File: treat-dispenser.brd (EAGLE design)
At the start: 88.9 x 44.5 mm, 32 parts, among them U1 MCP73831, U2 TPS6103x, Y1 16MHz

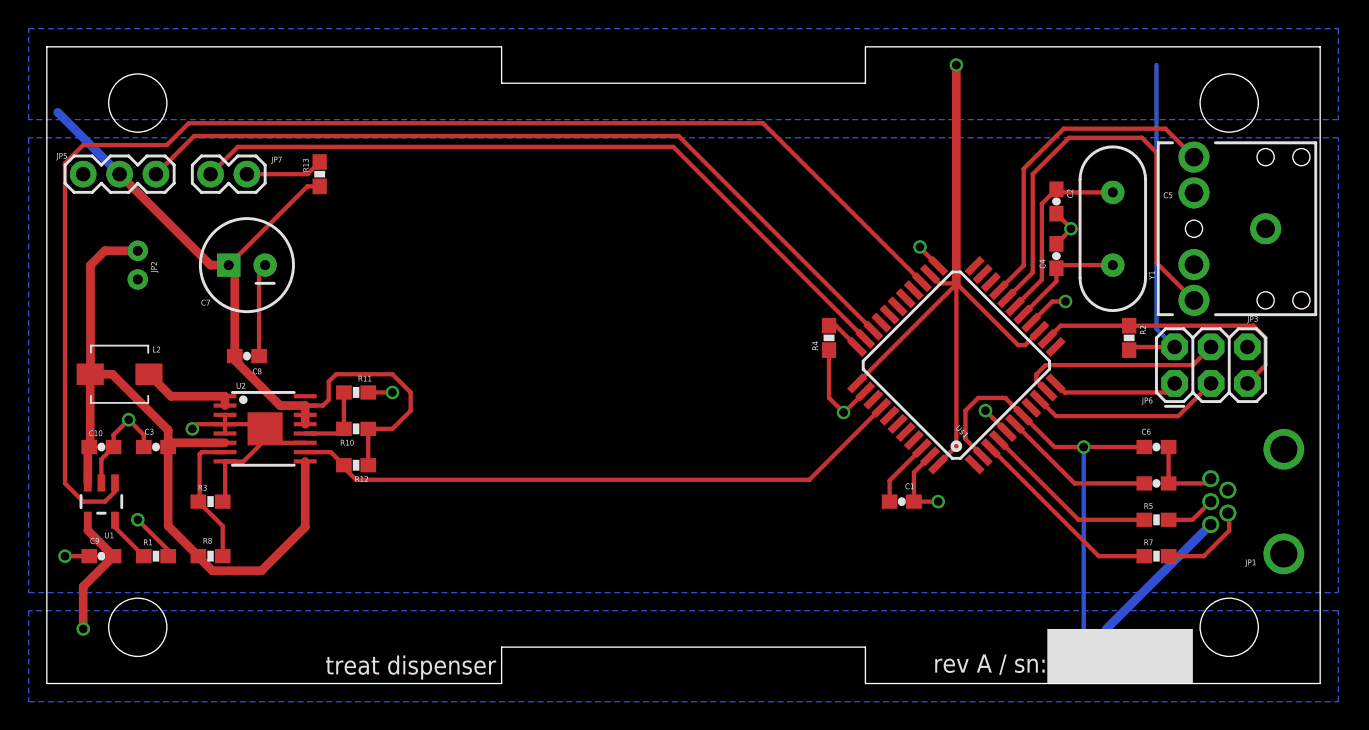
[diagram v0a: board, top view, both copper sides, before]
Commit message: moved servo to clear path for battery connector
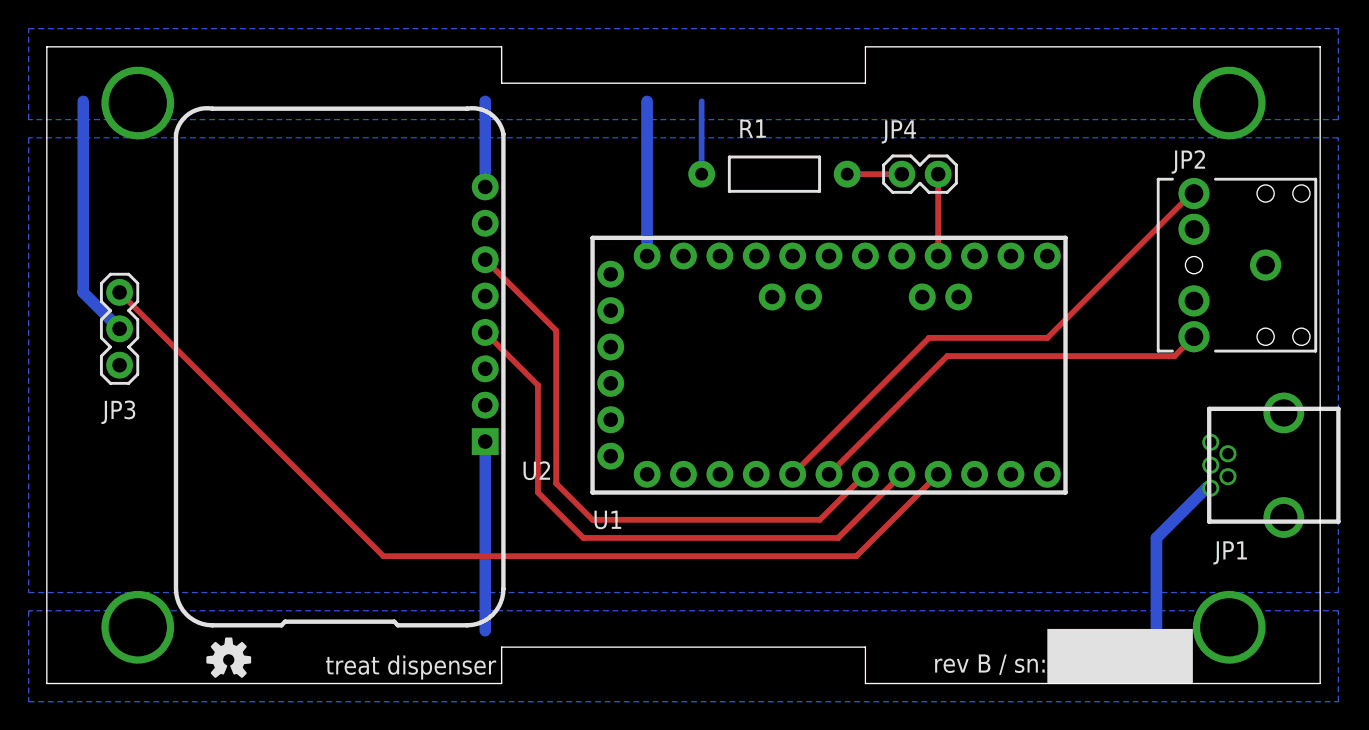
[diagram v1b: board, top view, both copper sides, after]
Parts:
- removed C1: 0.1uF, SparkFun:0603-CAP
- removed C10, C9: 4.7uF, SparkFun:0603-CAP
- removed C2, C4: 22pF, SparkFun:0603-CAP
- removed C3, C8: 10uF, SparkFun:0603-CAP
- removed C5, C6: 1uF, SparkFun:0603-CAP
- removed C7: 220uF, SparkFun-Capacitors:CPOL-RADIAL-100UF-25V
- removed JP5: (no value), SparkFun-Connectors:1X03
- removed JP6: (no value), SparkFun-Connectors:2X3
- removed JP7: (no value), SparkFun-Connectors:1X02
- removed L2: (no value), SparkFun-Passives:INDUCTOR-SRP4020
- removed R10, R12, R8: 1M, SparkFun:0603-RES
- removed R11: 110K, SparkFun:0603-RES
- removed R13: 470, SparkFun:0603-RES
- removed R2, R4: 10K, SparkFun:0603-RES
- removed R3: 182K, SparkFun:0603-RES
- removed R5, R7: 22, SparkFun:0603-RES
- removed U$1: ATMEGA32U4TQFP-44, SparkFun-DigitalIC:TQFP44
- removed Y1: 16MHz, SparkFun:HC49US
- added JP4: (no value), SparkFun-Connectors:1X02
- added LOGO1: OSHW-LOGOS, SparkFun-Aesthetics:OSHW-LOGO-S
- JP2: device SparkFun-Connectors:JST-2-PTH-KIT -> SparkFun-Connectors:AUDIO-JACK
- JP3: device SparkFun-Connectors:AUDIO-JACK -> SparkFun-Connectors:1X03
- R1: value 10K -> 470; device SparkFun:0603-RES -> SparkFun:AXIAL-0.4
- U1: value MCP73831 -> ARDUINO_PRO_MINI; device SparkFun:SOT23-5 -> SparkFun-Boards:ARDUINO_PRO_MINI
- U2: value TPS6103x -> PB1000; device tps6103x:TSSOP-16 -> powerboost:PB1000
- moved JP3 80.6 mm to (5.08, 22.2), turned to 90 degrees
- moved JP2 78.7 mm to (85.1, 29.2), turned to 180 degrees
- moved U1 51.7 mm to (54.6, 22.2), turned to 90 degrees
- moved R1 50.8 mm to (50.8, 35.6)
- moved U2 21.6 mm to (31.9, 4.06), turned to 90 degrees
- moved JP1 2.54 mm to (86.4, 15.2)
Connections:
- removed net A0: U$1.36
- removed net A1: R12.2, U$1.37, U2.10
- removed net A2: U$1.38
- removed net A3: U$1.39
- removed net A4: U$1.40
- removed net A5: U$1.41
- removed net AREF: C1.2, U$1.42
- removed net D+: JP1.D+, R5.2
- removed net D-: JP1.D-, R7.2
- removed net D10: U$1.30
- removed net D11: U$1.12
- removed net D12: U$1.26
- removed net D13: JP7.1, U$1.32
- removed net D14: U$1.8
- removed net D2: JP3.TIP, U$1.19
- removed net D3: JP3.RING, U$1.18
- removed net D4: U$1.25, U1.1
- removed net D5: JP5.3, U$1.31
- removed net D6: U$1.27
- removed net D7: U$1.1
- removed net D8: U$1.28
- removed net D9: U$1.29
- removed net FB: R10.2, R11.1, U2.12
- removed net LBI: R3.1, R8.1, U2.7
- removed net MISO: JP6.1, U$1.11
- removed net MOSI: JP6.4, U$1.10
- removed net N$1: C4.1, U$1.16, Y1.1
- removed net N$2: C2.1, U$1.17, Y1.2
- removed net N$3: U$1.22
- removed net N$4: C5.2, U$1.6
- removed net N$5: R4.2, U$1.33
- removed net PROG: R1.1, U1.5
- removed net RD+: R5.1, U$1.4
- removed net RD-: R7.1, U$1.3
- removed net RESET: JP6.5, R2.1, U$1.13
- removed net RXI: U$1.20
- removed net SCK: JP6.3, U$1.9
- removed net SW: L2.P$2, U2.1, U2.2
- removed net TXO: U$1.21
- removed net UVCC: C6.2, C9.1, JP1.VBUS, U$1.2, U$1.7, U1.4
- removed net VCC: C7.1, C8.1, JP5.2, JP6.2, R10.1, R12.1, R13.1, R2.2, U$1.14, U$1.24, U$1.34, U$1.44, U2.13, U2.14, U2.15
- removed net V_BATT: C10.1, C3.1, JP2.2, L2.P$1, R8.2, U1.3, U2.6, U2.9
- new net 5V: JP3.2, R1.P$1, U1.24, U2.P8
- new net B1: JP2.TIP, U1.5
- new net B2: JP2.RING, U1.6
- new net EN: U1.8, U2.P4
- new net LBO: U1.7, U2.P6
- new net LED: JP4.1, U1.16
- new net SERVO: JP3.3, U1.9
- new net VBUS: JP1.VBUS, U2.P1
- net GND: now also JP2.SLEEVE, JP3.1, U1.23, U1.4, U2.P5, U2.P7; no longer C1.1, C10.2, C2.2, C3.2, C4.2, C5.1, C6.1, C7.2, C8.2, C9.2, JP2.1, JP3.SLEEVE, JP5.1, JP6.6, R1.2, R11.2, R3.2, R4.1, U$1.15, U$1.23, U$1.35, U$1.43, U$1.5, U1.2, U2.11, U2.3, U2.4, U2.5, U2.8, U2.PAD
- net N$8: now also JP4.2, R1.P$2; no longer JP7.2, R13.2
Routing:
- net VCC: track 128.0 -> 0.00 mm, vias 1 -> 0
- net D4: track 93.2 -> 0.00 mm
- net SERVO: track 0.00 -> 67.1 mm
- net GND: track 65.3 -> 0.00 mm, vias 11 -> 0
- net D5: track 56.8 -> 0.00 mm
- net V_BATT: track 53.7 -> 0.00 mm
- net D13: track 52.0 -> 0.00 mm
- net UVCC: track 50.2 -> 0.00 mm, vias 2 -> 0
- net A1: track 43.2 -> 0.00 mm
- net LBO: track 0.00 -> 41.6 mm
- net EN: track 0.00 -> 41.3 mm
- net 5V: track 0.00 -> 38.8 mm
- net B1: track 0.00 -> 36.1 mm
- net D3: track 30.9 -> 0.00 mm
- net B2: track 0.00 -> 29.5 mm
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- added copper zone on layer 16, net 5V
- added copper zone on layer 16, net VBUS
- removed copper zone on layer 16, net UVCC
- removed copper zone on layer 16, net VCC
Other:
- outline, holes or cut-outs redrawn
- board text added: "rev B / sn:"
- board text removed: "rev A / sn:"

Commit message: rev C update: - added dedicated battery connector - reversed led polarity - added enable switch - removed en connection to arduino - added status led and lbo to arduino code
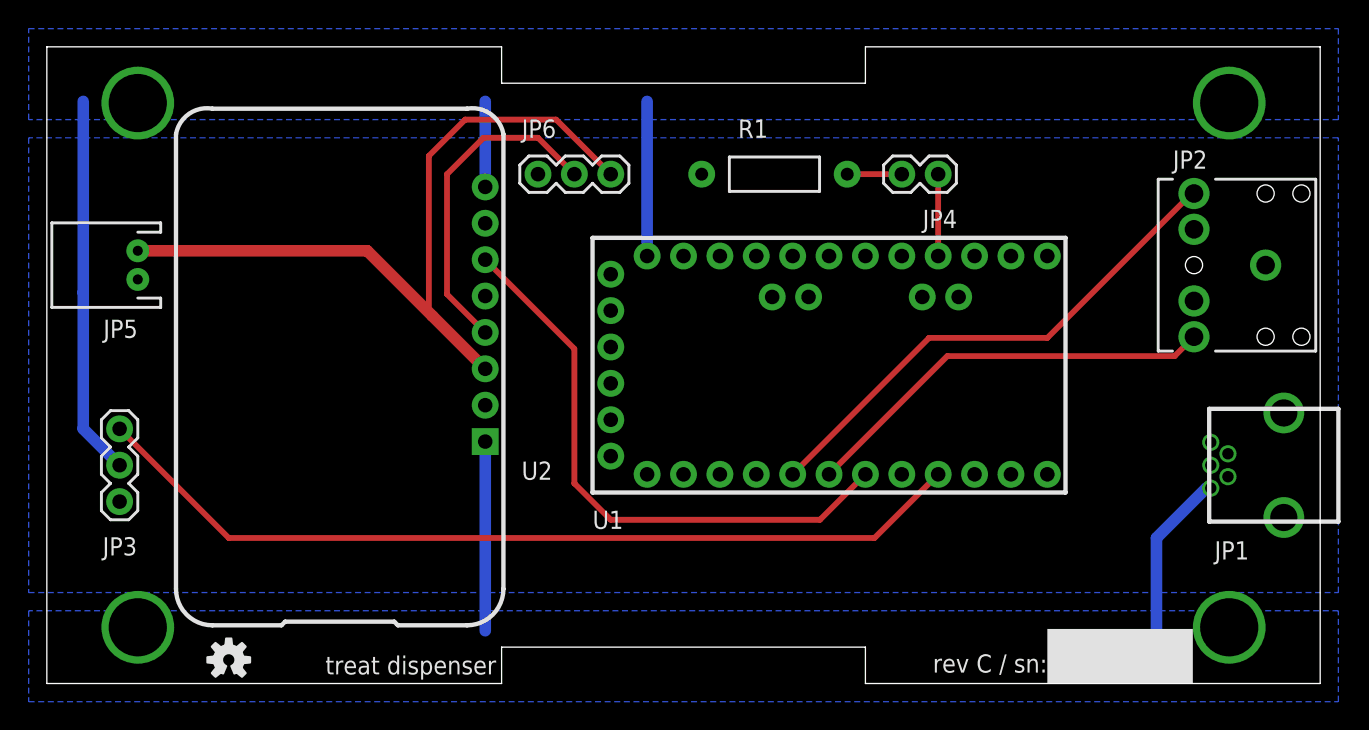
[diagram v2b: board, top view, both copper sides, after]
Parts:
- added JP5: (no value), SparkFun-Connectors:JST-2-PTH
- added JP6: (no value), SparkFun-Connectors:1X03
- moved JP3 9.53 mm to (5.08, 12.7)
- moved JP4 2.54 mm to (59.7, 35.6), turned to 0 degrees
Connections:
- removed net N$8: JP4.2, R1.P$2
- new net N$5: JP4.1, R1.P$2
- new net VBAT: JP5.2, JP6.3, U2.P3
- net 5V: no longer R1.P$1
- net EN: now also JP6.2; no longer U1.8
- net GND: now also JP5.1, JP6.1, R1.P$1
- net LED: now also JP4.2; no longer JP4.1
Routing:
- net VBAT: track 0.00 -> 54.3 mm
- net EN: track 41.3 -> 23.1 mm
- net SERVO: track 67.1 -> 62.1 mm
- net 5V: track 38.8 -> 43.2 mm
- net N$8: track 3.81 -> 0.00 mm
- net N$5: track 0.00 -> 3.81 mm
- net LBO: track 41.6 -> 40.9 mm
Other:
- board text added: "rev C / sn:"
- board text removed: "rev B / sn:"
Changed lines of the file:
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@@
 <board>
 <plain>
-<text x="69.85" y="2.032" size="1.27" layer="21" font="vector" rot="R180">rev B / sn:</text>
+<text x="69.85" y="2.032" size="1.27" layer="21" font="vector" rot="R180">rev C / sn:</text>
 <text x="31.369" y="1.905" size="1.27" layer="21" font="vector" rot="R180">treat dispenser</text>
 <rectangle x1="69.85" y1="0" x2="80.01" y2="3.81" layer="21" rot="R180"/>
@@
 <attribute name="VALUE" x="86.36" y="27.94" size="0.4064" layer="27" rot="R180"/>
 </element>
-<element name="JP3" library="SparkFun-Connectors" package="1X03" value="" x="5.08" y="22.225" smashed="yes" rot="R90">
-<attribute name="PN" value="952-1312-ND" x="5.08" y="22.225" size="1.778" layer="27" rot="R90" display="off"/>
-<attribute name="NAME" x="6.2992" y="18.4658" size="1.27" layer="25" font="vector" align="bottom-right"/>
-<attribute name="VALUE" x="8.255" y="20.955" size="1.27" layer="27" rot="R90"/>
-</element>
-<element name="JP4" library="SparkFun-Connectors" package="1X02" value="" x="62.23" y="35.56" smashed="yes" rot="R180">
-<attribute name="PN" value="952-1311-ND" x="62.23" y="35.56" size="1.778" layer="27" rot="R180" display="off"/>
-<attribute name="NAME" x="58.3692" y="38.0492" size="1.27" layer="25" font="vector"/>
-<attribute name="VALUE" x="63.5" y="38.735" size="1.27" layer="27" rot="R180"/>
+<element name="JP3" library="SparkFun-Connectors" package="1X03" value="" x="5.08" y="12.7" smashed="yes" rot="R90">
+<attribute name="PN" value="952-1312-ND" x="5.08" y="12.7" size="1.778" layer="27" rot="R90" display="off"/>
+<attribute name="NAME" x="6.2992" y="8.9408" size="1.27" layer="25" font="vector" align="bottom-right"/>
+<attribute name="VALUE" x="8.255" y="11.43" size="1.27" layer="27" rot="R90"/>
+</element>
+<element name="JP4" library="SparkFun-Connectors" package="1X02" value="" x="59.69" y="35.56" smashed="yes">
+<attribute name="PN" value="952-1311-ND" x="59.69" y="35.56" size="1.778" layer="27" display="off"/>
+<attribute name="NAME" x="63.5508" y="33.0708" size="1.27" layer="25" font="vector" rot="R180"/>
+<attribute name="VALUE" x="58.42" y="32.385" size="1.27" layer="27"/>
 </element>
 <element name="R1" library="SparkFun" package="AXIAL-0.4" value="470" x="50.8" y="35.56" smashed="yes">
@@
 </element>
 <element name="LOGO1" library="SparkFun-Aesthetics" package="OSHW-LOGO-S" value="OSHW-LOGOS" x="12.7" y="1.651"/>
+<element name="JP5" library="SparkFun-Connectors" package="JST-2-PTH" value="" x="6.35" y="29.21" smashed="yes" rot="R90">
+<attribute name="SKU" value="PRT-09914" x="6.35" y="29.21" size="1.778" layer="27" rot="R90" display="off"/>
+<attribute name="PROD_ID" value="CONN-09863" x="6.35" y="29.21" size="1.778" layer="27" rot="R90" display="off"/>
+<attribute name="NAME" x="6.35" y="25.4" size="1.27" layer="25" font="vector" rot="R180"/>
+<attribute name="VALUE" x="2.35" y="27.94" size="0.4064" layer="27" rot="R90"/>
+<attribute name="PN" value="455-1719-ND" x="6.35" y="29.21" size="1.778" layer="27" rot="R90" display="off"/>
+</element>
+<element name="JP6" library="SparkFun-Connectors" package="1X03" value="" x="34.29" y="35.56" smashed="yes">
+<attribute name="PN" value="EG1903-ND" x="34.29" y="35.56" size="1.778" layer="27" display="off"/>
+<attribute name="NAME" x="35.56" y="39.37" size="1.27" layer="25" font="vector" rot="R180"/>
+<attribute name="VALUE" x="33.02" y="32.385" size="1.27" layer="27"/>
+</element>
 </elements>
 <signals>
@@
 <contactref element="U2" pad="P7"/>
 <contactref element="JP1" pad="GND"/>
+<contactref element="R1" pad="P$1"/>
+<contactref element="JP5" pad="1"/>
+<contactref element="JP6" pad="1"/>
 </signal>
 <signal name="SERVO">
 <contactref element="JP3" pad="3"/>
 <contactref element="U1" pad="9"/>
-<wire x1="62.23" y1="14.605" x2="56.515" y2="8.89" width="0.4064" layer="1"/>
-<wire x1="5.08" y1="27.305" x2="23.495" y2="8.89" width="0.4064" layer="1"/>
-<wire x1="23.495" y1="8.89" x2="56.515" y2="8.89" width="0.4064" layer="1"/>
+<wire x1="62.23" y1="14.605" x2="57.785" y2="10.16" width="0.4064" layer="1"/>
+<wire x1="57.785" y1="10.16" x2="12.7" y2="10.16" width="0.4064" layer="1"/>
+<wire x1="5.08" y1="17.78" x2="12.7" y2="10.16" width="0.4064" layer="1"/>
 </signal>
 <signal name="N$9">
 </signal>
 <signal name="N$10">
-</signal>
-<signal name="N$8">
-<contactref element="R1" pad="P$2"/>
-<contactref element="JP4" pad="2"/>
-<wire x1="59.69" y1="35.56" x2="55.88" y2="35.56" width="0.4064" layer="1"/>
 </signal>
 <signal name="5V">
 <contactref element="JP3" pad="2"/>
 <contactref element="U2" pad="P8"/>
-<contactref element="R1" pad="P$1"/>
 <contactref element="U1" pad="24"/>
 <polygon width="0.3556" layer="16">
@@
 </polygon>
 <wire x1="41.91" y1="29.845" x2="41.91" y2="40.64" width="0.8128" layer="16"/>
-<wire x1="45.72" y1="35.56" x2="45.72" y2="40.64" width="0.4064" layer="16"/>
 <wire x1="30.607" y1="34.671" x2="30.607" y2="40.64" width="0.8128" layer="16"/>
-<wire x1="5.08" y1="24.765" x2="2.54" y2="27.305" width="0.8128" layer="16"/>
 <wire x1="2.54" y1="27.305" x2="2.54" y2="40.64" width="0.8128" layer="16"/>
+<wire x1="2.54" y1="27.305" x2="2.54" y2="17.78" width="0.8128" layer="16"/>
+<wire x1="2.54" y1="17.78" x2="5.08" y2="15.24" width="0.8128" layer="16"/>
 </signal>
 <signal name="B2">
@@
 </signal>
 <signal name="LED">
-<contactref element="JP4" pad="1"/>
 <contactref element="U1" pad="16"/>
+<contactref element="JP4" pad="2"/>
 <wire x1="62.23" y1="35.56" x2="62.23" y2="29.845" width="0.4064" layer="1"/>
 </signal>
@@
 <contactref element="U1" pad="7"/>
 <wire x1="57.15" y1="14.605" x2="53.975" y2="11.43" width="0.4064" layer="1"/>
-<wire x1="30.607" y1="29.591" x2="35.56" y2="24.638" width="0.4064" layer="1"/>
-<wire x1="35.56" y1="24.638" x2="35.56" y2="13.97" width="0.4064" layer="1"/>
-<wire x1="53.975" y1="11.43" x2="38.1" y2="11.43" width="0.4064" layer="1"/>
-<wire x1="38.1" y1="11.43" x2="35.56" y2="13.97" width="0.4064" layer="1"/>
-</signal>
-<signal name="EN">
-<contactref element="U2" pad="P4"/>
-<contactref element="U1" pad="8"/>
-<wire x1="59.69" y1="14.605" x2="55.245" y2="10.16" width="0.4064" layer="1"/>
-<wire x1="30.607" y1="24.511" x2="34.29" y2="20.828" width="0.4064" layer="1"/>
-<wire x1="55.245" y1="10.16" x2="37.465" y2="10.16" width="0.4064" layer="1"/>
-<wire x1="37.465" y1="10.16" x2="34.29" y2="13.335" width="0.4064" layer="1"/>
-<wire x1="34.29" y1="13.335" x2="34.29" y2="20.828" width="0.4064" layer="1"/>
+<wire x1="53.975" y1="11.43" x2="39.37" y2="11.43" width="0.4064" layer="1"/>
+<wire x1="39.37" y1="11.43" x2="36.83" y2="13.97" width="0.4064" layer="1"/>
+<wire x1="36.83" y1="13.97" x2="36.83" y2="23.368" width="0.4064" layer="1"/>
+<wire x1="36.83" y1="23.368" x2="30.607" y2="29.591" width="0.4064" layer="1"/>
+</signal>
+<signal name="VBAT">
+<contactref element="U2" pad="P3"/>
+<contactref element="JP5" pad="2"/>
+<contactref element="JP6" pad="3"/>
+<wire x1="6.35" y1="30.21" x2="22.368" y2="30.21" width="0.8128" layer="1"/>
+<wire x1="22.368" y1="30.21" x2="26.924" y2="25.654" width="0.8128" layer="1"/>
+<wire x1="26.924" y1="25.654" x2="30.607" y2="21.971" width="0.8128" layer="1"/>
+<wire x1="26.67" y1="36.83" x2="26.67" y2="25.908" width="0.4064" layer="1"/>
+<wire x1="26.67" y1="25.908" x2="26.924" y2="25.654" width="0.4064" layer="1"/>
+<wire x1="26.67" y1="36.83" x2="29.21" y2="39.37" width="0.4064" layer="1"/>
+<wire x1="29.21" y1="39.37" x2="35.56" y2="39.37" width="0.4064" layer="1"/>
+<wire x1="35.56" y1="39.37" x2="39.37" y2="35.56" width="0.4064" layer="1"/>
 </signal>
 <signal name="VBUS">
@@
 <via x="6.35" y="3.9243" extent="1-16" drill="4.064"/>
 </signal>
+<signal name="EN">
+<contactref element="U2" pad="P4"/>
+<contactref element="JP6" pad="2"/>
+<wire x1="27.94" y1="35.56" x2="27.94" y2="27.178" width="0.4064" layer="1"/>
+<wire x1="27.94" y1="27.178" x2="30.607" y2="24.511" width="0.4064" layer="1"/>
+<wire x1="36.83" y1="35.56" x2="34.29" y2="38.1" width="0.4064" layer="1"/>
+<wire x1="34.29" y1="38.1" x2="30.48" y2="38.1" width="0.4064" layer="1"/>
+<wire x1="30.48" y1="38.1" x2="27.94" y2="35.56" width="0.4064" layer="1"/>
+</signal>
+<signal name="N$5">
+<contactref element="R1" pad="P$2"/>
+<contactref element="JP4" pad="1"/>
+<wire x1="55.88" y1="35.56" x2="59.69" y2="35.56" width="0.4064" layer="1"/>
+</signal>
 </signals>
